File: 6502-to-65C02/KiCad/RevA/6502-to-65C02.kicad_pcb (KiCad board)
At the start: 2 copper layers, 52 x 32 mm, 5 parts

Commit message: Initial design
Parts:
- added C2: 100nF, Capacitor_SMD:C_0402_1005Metric_Pad0.74x0.62mm_HandSolder, F.Cu at (102.6, 59.2)
- C1: value 10µF -> 100nF; footprint Capacitor_THT:CP_Radial_D5.0mm_P2.50mm -> Capacitor_SMD:C_0402_1005Metric_Pad0.74x0.62mm_HandSolder
- R1: footprint Resistor_THT:R_Axial_DIN0207_L6.3mm_D2.5mm_P7.62mm_Horizontal -> Resistor_SMD:R_0402_1005Metric_Pad0.72x0.64mm_HandSolder
- UE10: footprint Package_DIP:DIP-40_W15.24mm_Socket -> Package_DIP:DIP-40_W15.24mm
- UE101: footprint Package_DIP:DIP-40_W15.24mm -> Package_DIP:DIP-40_W15.24mm_Socket
- moved R1 41.1 mm to (117.6, 59.2)
- moved UE102 40.2 mm to (83.2, 63.1), turned to -90 degrees
- moved UE101 36.5 mm to (121.0, 54.0)
- moved UE10 36.4 mm to (121.1, 57.0)
- moved C1 28.9 mm to (87.4, 65.5), turned to 90 degrees
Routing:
- net GND: track 39.4 -> 4.05 mm, vias 2 -> 4
- net /D1: track 11.9 -> 42.3 mm
- net /D2: track 11.5 -> 0.00 mm, vias 1 -> 0
- net Net-(UE101-D4): track 6.88 -> 14.9 mm
- net /D0: track 14.6 -> 22.4 mm
- net Net-(UE101-D3): track 8.70 -> 16.3 mm, vias 1 -> 0
- net Net-(UE101-D5): track 6.83 -> 14.1 mm
- net RDY: track 11.4 -> 5.42 mm
- net Net-(UE101-D6): track 7.77 -> 13.4 mm
- net /D7: track 14.5 -> 9.19 mm, vias 0 -> 1
- net Net-(UE101-D2): track 13.1 -> 18.2 mm, vias 1 -> 0
- net /D6: track 15.4 -> 10.6 mm
- net Net-(UE101-D7): track 7.23 -> 11.1 mm, vias 0 -> 1
- net Net-(UE101-D1): track 23.3 -> 20.0 mm, vias 1 -> 0
- net +5V: track 32.7 -> 36.0 mm
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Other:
- board size 52 x 32 mm -> 54 x 23 mm

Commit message: Finalised design for testing
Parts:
- moved C1 58.9 mm to (146.0, 71.6), turned to -90 degrees
- moved UE10 43.5 mm to (163.0, 68.8)
- moved UE101 43.5 mm to (163.1, 65.0)
- moved R1 43.4 mm to (159.4, 71.0)
- moved UE102 42.2 mm to (123.9, 74.2)
- moved C2 30.8 mm to (128.3, 76.2), turned to 90 degrees
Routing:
- net /D2: track 0.00 -> 24.5 mm, vias 0 -> 1
- net /D1: track 42.3 -> 21.5 mm, vias 1 -> 0
- net +5V: track 36.0 -> 50.4 mm
- net /D7: track 9.19 -> 19.4 mm, vias 1 -> 0
- net /D6: track 10.6 -> 18.0 mm
- net GND: track 4.05 -> 10.9 mm, vias 4 -> 6
- net R/W: track 26.7 -> 33.4 mm, vias 0 -> 1
- net /D5: track 13.8 -> 16.6 mm, vias 1 -> 0
- net Net-(UE101-D7): track 11.1 -> 13.9 mm
- net Net-(UE101-D3): track 16.3 -> 18.9 mm, vias 0 -> 1
- net Net-(UE101-D0): track 21.9 -> 24.2 mm, vias 0 -> 1
- net Net-(UE101-D1): track 20.0 -> 21.3 mm, vias 0 -> 1
- net Net-(UE101-D2): track 18.2 -> 19.4 mm, vias 0 -> 1
- net Net-(UE101-D5): track 14.1 -> 15.2 mm, vias 0 -> 1
- net /D0: track 22.4 -> 23.3 mm
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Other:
- board size 54 x 23 mm -> 54 x 24 mm
- board text added: "6502 to 65C02 For VIC-20 © 2025"
- board text added: "A11 A10 A9 A8 A7 A6 A5 A4 A3 A2 A1 A0 +5V SYNC ~{NMI} ~{IRQ} Φ1 RDY"
- board text added: "Brett Hallen, Apr 2025 Port Macquarie, Australia www.youtube.com/@Brfff"
- board text added: "GND A12 A13 A14 A15 D7 D6 D5 D4 D3 D2 D1 D0 R/~{W} Φ0 SO Φ2 RESET"

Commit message: Cosmetic changes, additional documentation
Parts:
- moved UE101 48.5 mm to (115.9, 53.5)
- moved C1 48.5 mm to (98.8, 60.1)
- moved C2 48.5 mm to (81.1, 64.7)
- moved R1 48.5 mm to (112.2, 59.5)
- moved UE10 48.5 mm to (115.8, 57.3)
- moved UE102 48.5 mm to (76.8, 62.7)
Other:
- board text added: "6502 to W65C02S For VIC-20 © 2025"
- board text removed: "6502 to 65C02 For VIC-20 © 2025"

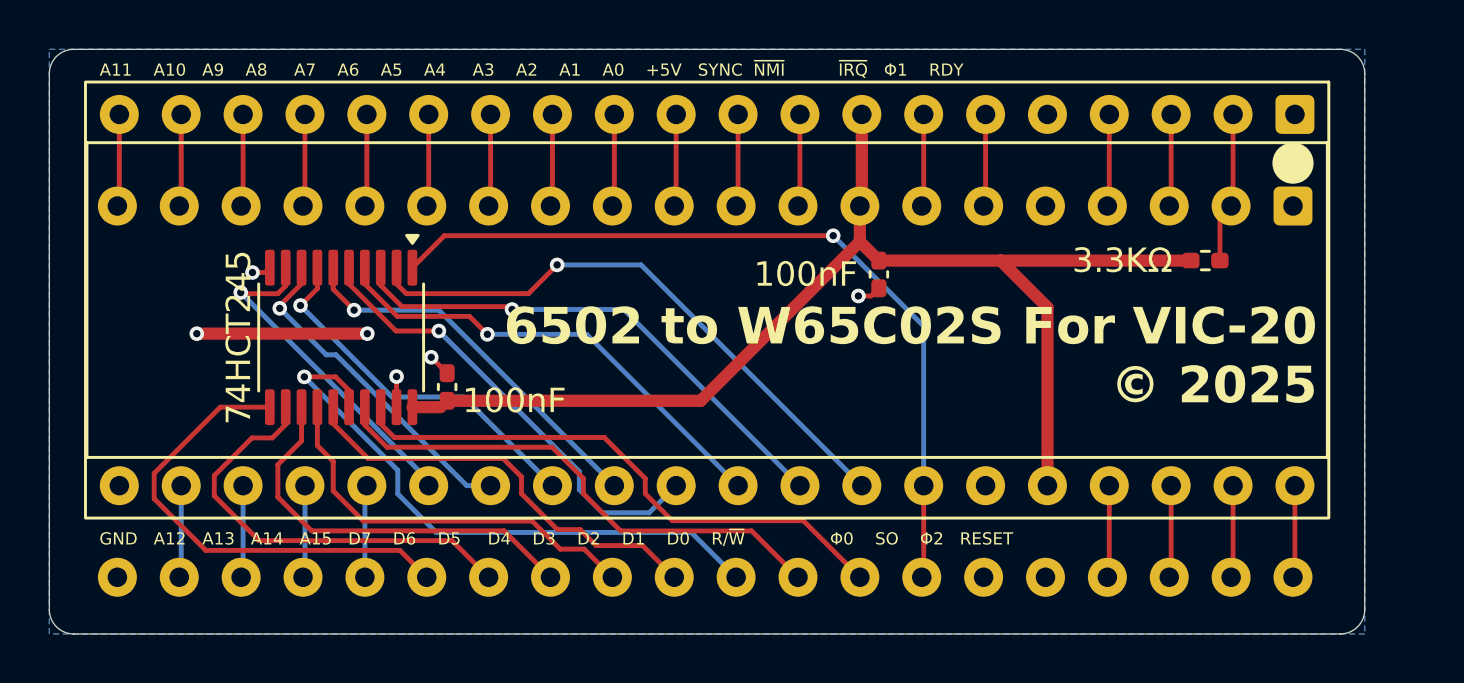
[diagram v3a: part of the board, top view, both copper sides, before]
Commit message: Corrected 74LS245 orientation
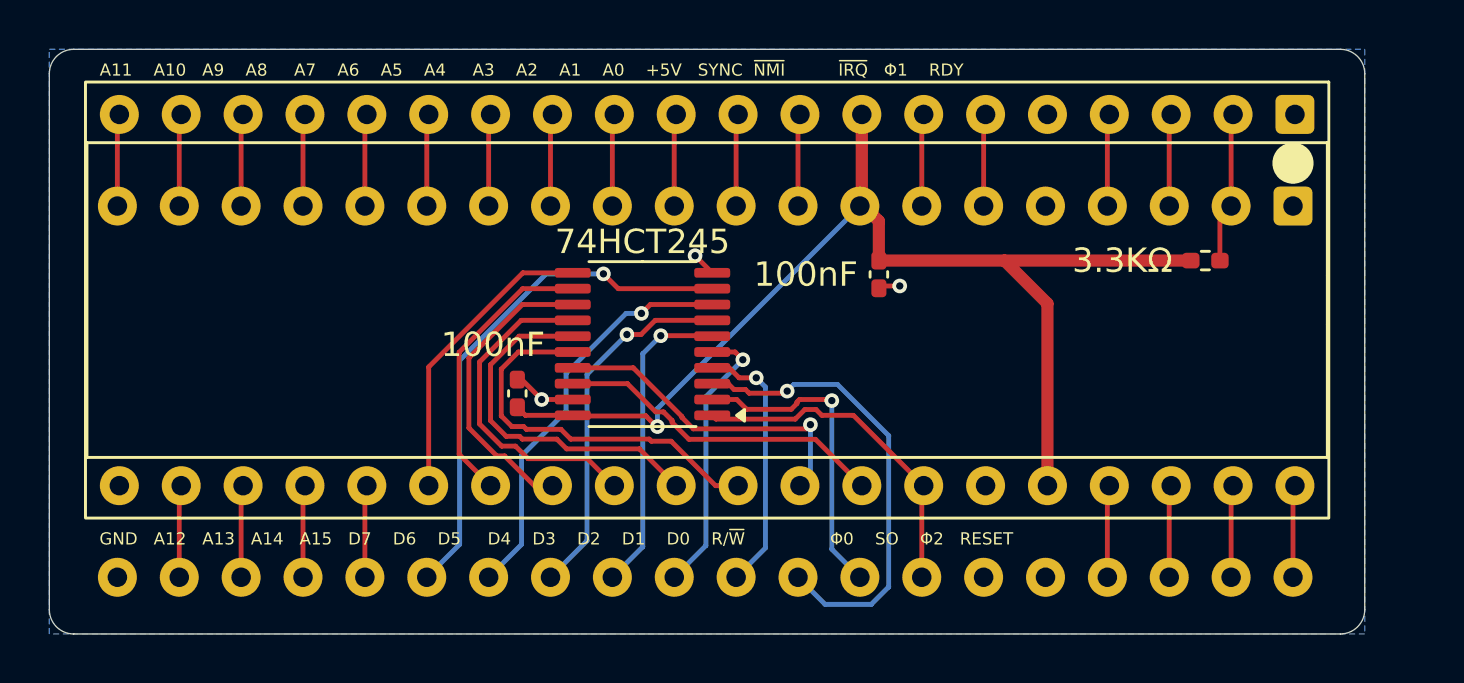
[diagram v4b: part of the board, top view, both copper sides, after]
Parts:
- UE101: value 65C02S -> W65C02S
- moved UE102 12.4 mm to (89.1, 63.0), turned to 180 degrees
- moved C2 2.89 mm to (84.0, 65.0)
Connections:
- UE102 pad 11: /D7 -> Net-(UE101-D7)
- UE102 pad 12: /D6 -> Net-(UE101-D6)
- UE102 pad 13: /D5 -> Net-(UE101-D5)
- UE102 pad 14: /D4 -> Net-(UE101-D4)
- UE102 pad 15: /D3 -> Net-(UE101-D3)
- UE102 pad 16: /D2 -> Net-(UE101-D2)
- UE102 pad 17: /D1 -> Net-(UE101-D1)
- UE102 pad 18: /D0 -> Net-(UE101-D0)
- UE102 pad 2: Net-(UE101-D0) -> /D0
- UE102 pad 3: Net-(UE101-D1) -> /D1
- UE102 pad 4: Net-(UE101-D2) -> /D2
- UE102 pad 5: Net-(UE101-D3) -> /D3
- UE102 pad 6: Net-(UE101-D4) -> /D4
- UE102 pad 7: Net-(UE101-D5) -> /D5
- UE102 pad 8: Net-(UE101-D6) -> /D6
- UE102 pad 9: Net-(UE101-D7) -> /D7
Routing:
- net R/W: track 33.4 -> 14.0 mm, vias 1 -> 0
- net /D2: track 24.5 -> 10.8 mm
- net Net-(UE101-D0): track 24.2 -> 13.6 mm, vias 1 -> 0
- net /D0: track 23.3 -> 13.0 mm, vias 0 -> 1
- net Net-(UE101-D1): track 21.3 -> 13.6 mm
- net GND: track 10.9 -> 4.50 mm, vias 6 -> 3
- net /D3: track 17.7 -> 11.5 mm, vias 0 -> 1
- net Net-(UE101-D3): track 18.9 -> 14.9 mm, vias 1 -> 0
- net /D4: track 16.6 -> 12.9 mm, vias 0 -> 1
- net Net-(UE101-D2): track 19.4 -> 16.1 mm, vias 1 -> 0
- net Net-(UE101-D5): track 15.2 -> 12.5 mm, vias 1 -> 0
- net +5V: track 50.4 -> 47.9 mm, vias 0 -> 1
- net /D1: track 21.5 -> 19.1 mm, vias 0 -> 1
- net /D7: track 19.4 -> 21.6 mm, vias 0 -> 1
- net Net-(UE101-D4): track 15.8 -> 13.7 mm, vias 1 -> 0
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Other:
- board text removed: "6502 to W65C02S For VIC-20 © 2025"

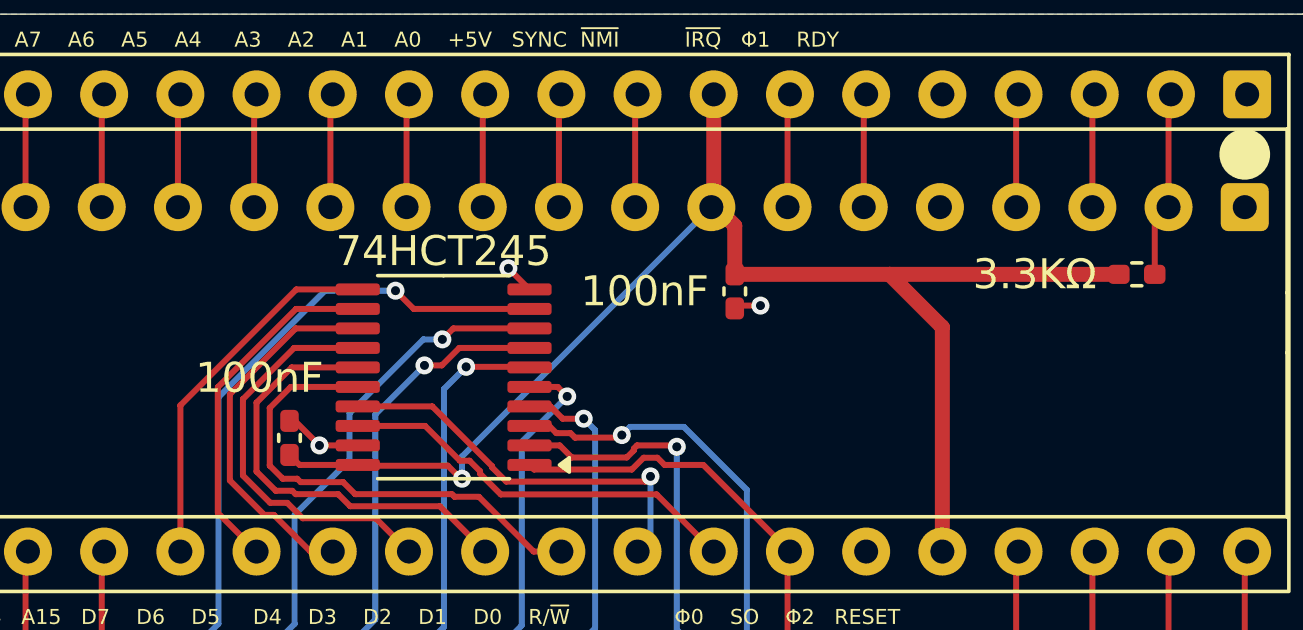
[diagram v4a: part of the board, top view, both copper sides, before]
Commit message: Sent for test fabrication
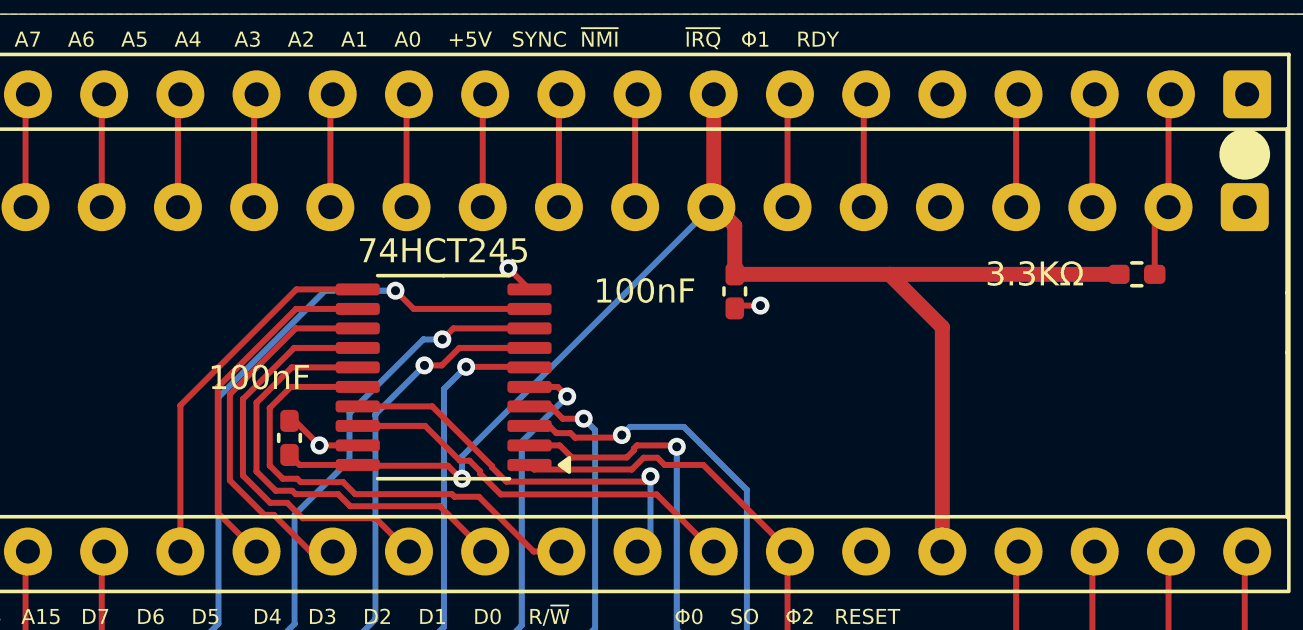
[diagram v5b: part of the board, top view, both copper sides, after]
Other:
- board text added: "Brett Hallen Port Macquarie, Australia www.youtube.com/@Brfff"
- board text removed: "Brett Hallen, Apr 2025 Port Macquarie, Australia www.youtube.com/@Brfff"
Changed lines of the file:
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@@
 			(effects
 				(font
-					(size 1 1)
-					(thickness 0.15)
+					(size 0.8 0.8)
+					(thickness 0.1)
 				)
 			)
@@
 			(effects
 				(font
-					(size 1 1)
-					(thickness 0.15)
+					(size 0.8 0.8)
+					(thickness 0.1)
 				)
 			)
@@
 			(effects
 				(font
-					(size 1 1)
-					(thickness 0.15)
+					(size 0.8 0.8)
+					(thickness 0.1)
 				)
 			)
@@
 			(effects
 				(font
-					(size 1 1)
-					(thickness 0.15)
+					(size 0.8 0.8)
+					(thickness 0.1)
 				)
 			)
@@
 		)
 	)
-	(gr_text "Brett Hallen, Apr 2025\nPort Macquarie, Australia\nwww.youtube.com/@Brfff"
+	(gr_text "Brett Hallen\nPort Macquarie, Australia\nwww.youtube.com/@Brfff"
 		(at 116.8417 66.5473 0)
 		(layer "B.SilkS")
@@
 			(font
 				(size 1.5 1.5)
-				(thickness 0.3)
-				(bold yes)
+				(thickness 0.15)
 			)
 			(justify left bottom mirror)
 		)
 	)
-	(gr_text_box "6502 to W65C02S For VIC-20\n© 2025"
+	(gr_text_box "6502 to W65C02S For VIC-20\n(May 2025)"
 		(start 67 59)
 		(end 85 67)
@@
 		(border no)
 		(stroke
-			(width 0.1)
+			(width 0)
 			(type solid)
 		)
